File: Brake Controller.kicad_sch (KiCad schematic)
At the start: 21 parts, among them M1 12V, SW1 ENABLE, SW2 HSS, SW3 HSS, U1 IFX007T, U2 IFX007T

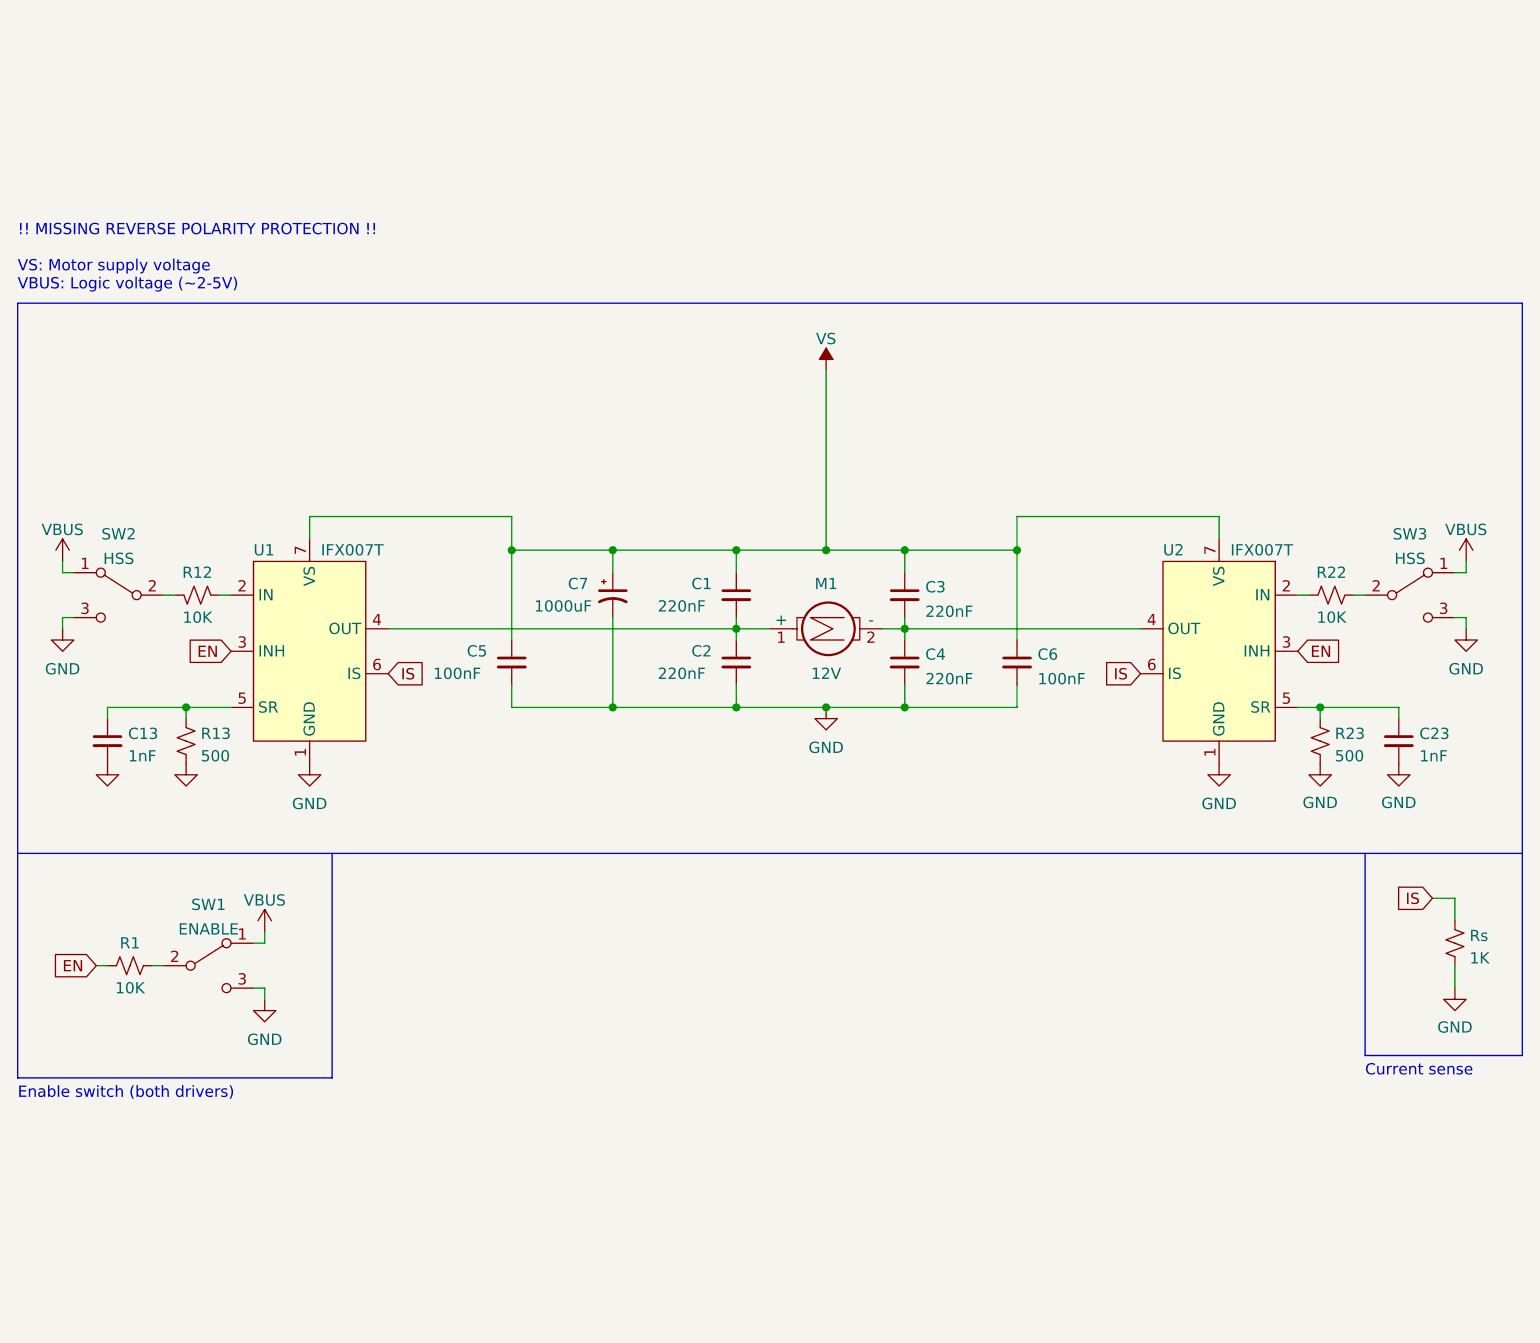
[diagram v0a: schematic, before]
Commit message: Add pin headers, prepare for PCB layout
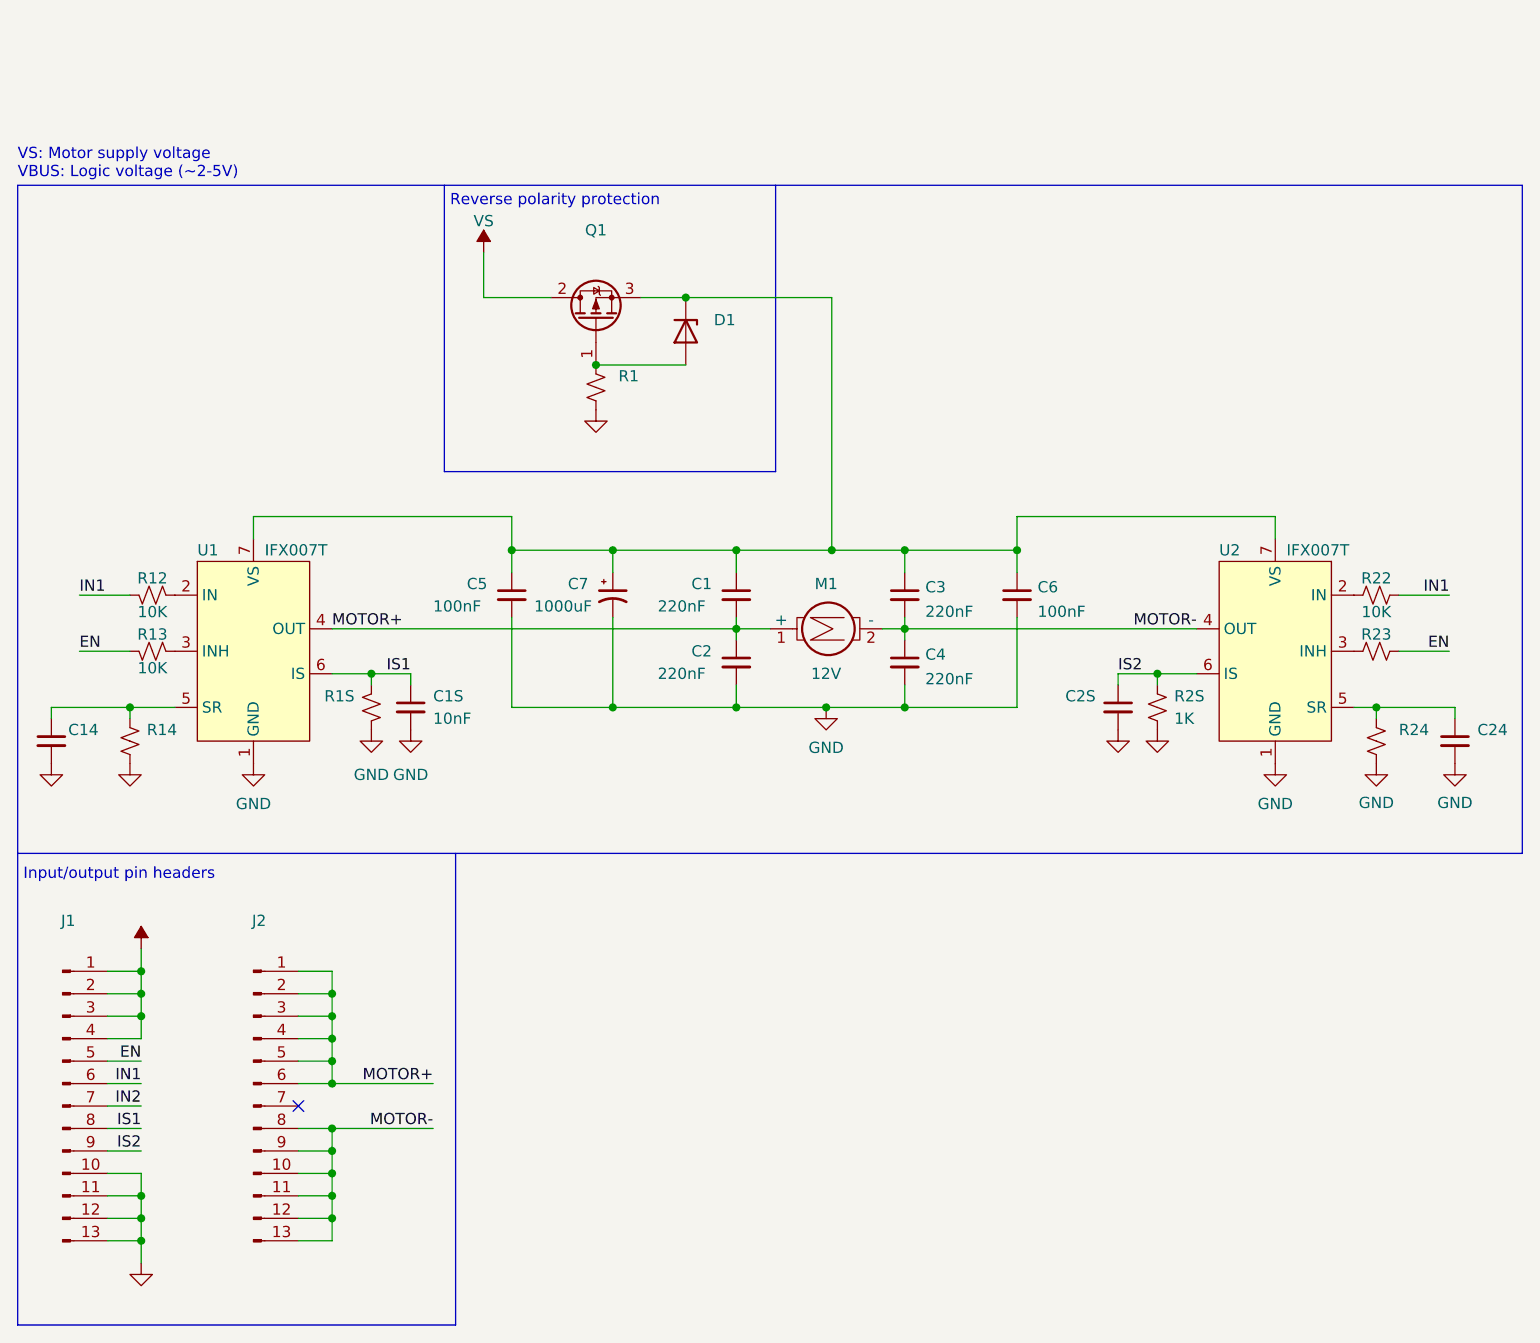
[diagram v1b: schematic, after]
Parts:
- removed C13, C23: 1nF, symbol Device:C_Small
- removed SW1: ENABLE, symbol Switch:SW_SPDT
- removed SW2, SW3: HSS, symbol Switch:SW_SPDT
- added C14, C24, C2S: (no value), symbol Device:C_Small
- added C1S: 10nF, symbol Device:C_Small
- added D1: (no value), symbol Device:D_Zener
- added J1, J2: (no value), symbol Connector:Conn_01x13_Male
- added Q1: (no value), symbol Device:Q_PMOS_GDS
- added R14, R1S, R24: (no value), symbol Device:R_Small_US
- R1: value 10K -> (none)
- R13: value 500 -> 10K
- R23: value 500 -> (none)
- renumbered Rs to R2S
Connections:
- net EN: now also R13.2, R23.2, J1.5 (Pin_5); no longer R1.1, U1.3 (INH), U2.3 (INH)
- net GND: now also R1.2, C14.2, C1S.2, C24.2, C2S.2, J1.10 (Pin_10), J1.11 (Pin_11), J1.12 (Pin_12), J1.13 (Pin_13), R14.2, R1S.2, R24.2; no longer R13.2, R23.2
- net VS: now also J1.1 (Pin_1), J1.2 (Pin_2), J1.3 (Pin_3), J1.4 (Pin_4), Q1.2 (D); no longer C1.1, C3.1, C5.1, C6.1, C7.1, U1.7 (VS), U2.7 (VS)
- net IN1: now reaches R12.2
- net IN1: now also R22.2, J1.6 (Pin_6)
- net at U2.5 (SR): now also C24.1, R24.1; no longer R23.1
- net MOTOR+: now reaches C1.2, C2.1, M1.1 (+), U1.4 (OUT)
- net MOTOR+: now also J2.1 (Pin_1), J2.2 (Pin_2), J2.3 (Pin_3), J2.4 (Pin_4), J2.5 (Pin_5), J2.6 (Pin_6)
- net MOTOR-: now reaches C3.2, C4.1, M1.2 (-), U2.4 (OUT)
- net MOTOR-: now also J2.10 (Pin_10), J2.11 (Pin_11), J2.12 (Pin_12), J2.13 (Pin_13), J2.8 (Pin_8), J2.9 (Pin_9)
- net at U1.5 (SR): now also C14.1, R14.1; no longer R13.1
- net IS renamed IS2
- net IS2: now also C2S.1, J1.9 (Pin_9); no longer U1.6 (IS)
- new net: D1.2 (A), Q1.1 (G), R1.1
- new net: C1.1, C3.1, C5.1, C6.1, C7.1, D1.1 (K), Q1.3 (S), U1.7 (VS), U2.7 (VS)
- new net: R13.1, U1.3 (INH)
- new net: R23.1, U2.3 (INH)
- new net IN2: J1.7 (Pin_7)
- new net IS1: C1S.1, J1.8 (Pin_8), R1S.1, U1.6 (IS)
- no-connect marks 0 -> 1
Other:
- note added: "Input/output pin headers"
- note added: "Reverse polarity protection"
- note added: "VS: Motor supply voltage VBUS: Logic voltage (~2-5V)"
- note removed: "!! MISSING REVERSE POLARITY PROTECTION !! VS: Motor supply voltage VBUS: Logic voltage (~2-5V)"
- note removed: "Current sense"
- note removed: "Enable switch (both drivers)"
- moved on the sheet: C5, C6, R12, R22, R2S, U1, U2

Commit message: Edit author/schematic title
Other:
- company: Ben Owen -> AMP Purdue
- title: IFX007T Motor Driver Testing -> Brake Controller Breakout
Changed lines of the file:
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@@
   (paper "USLetter")
   (title_block
-    (title "IFX007T Motor Driver Testing")
-    (date "2022-01-06")
+    (title "Brake Controller Breakout")
+    (date "2022-04-04")
     (rev "A")
-    (company "Ben Owen")
+    (company "AMP Purdue")
   )
   (junction (at 207.01 104.14) (diameter 0) (color 0 0 0 0)

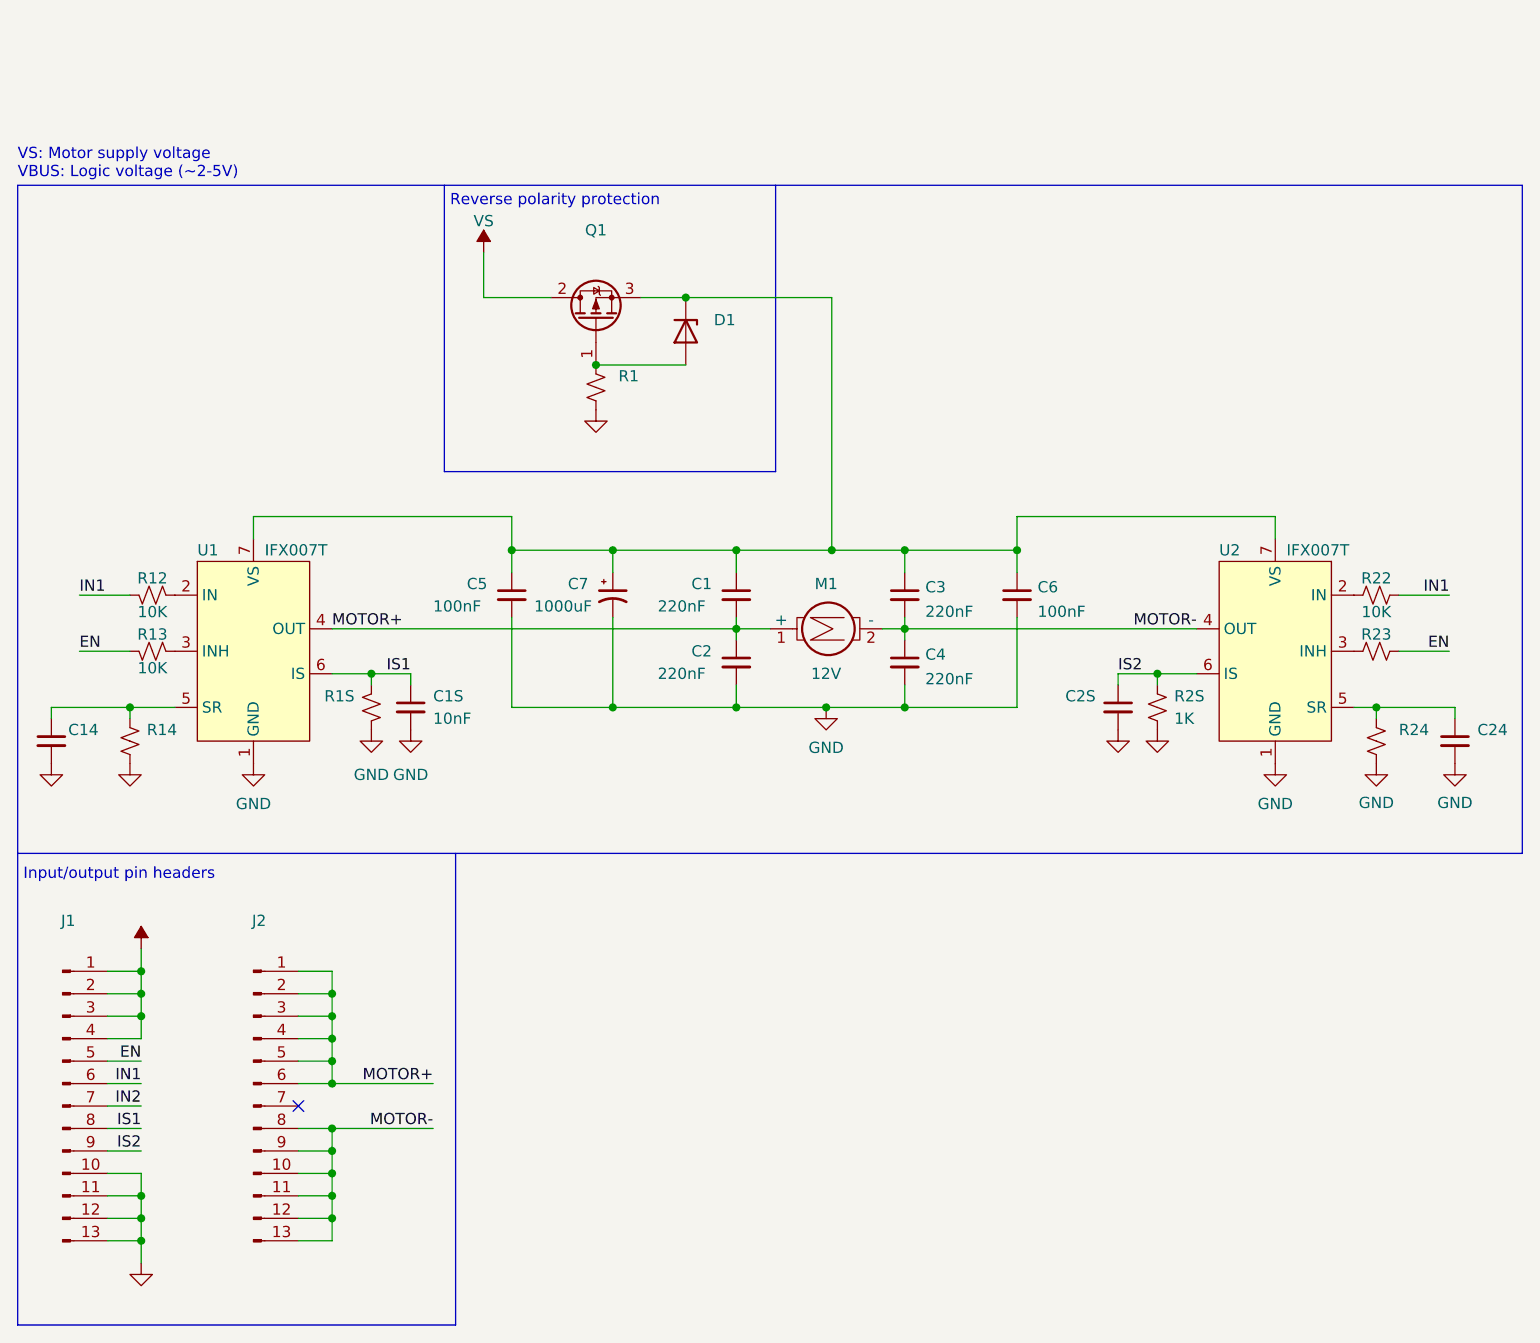
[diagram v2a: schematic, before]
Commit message: Fix missing GND labels
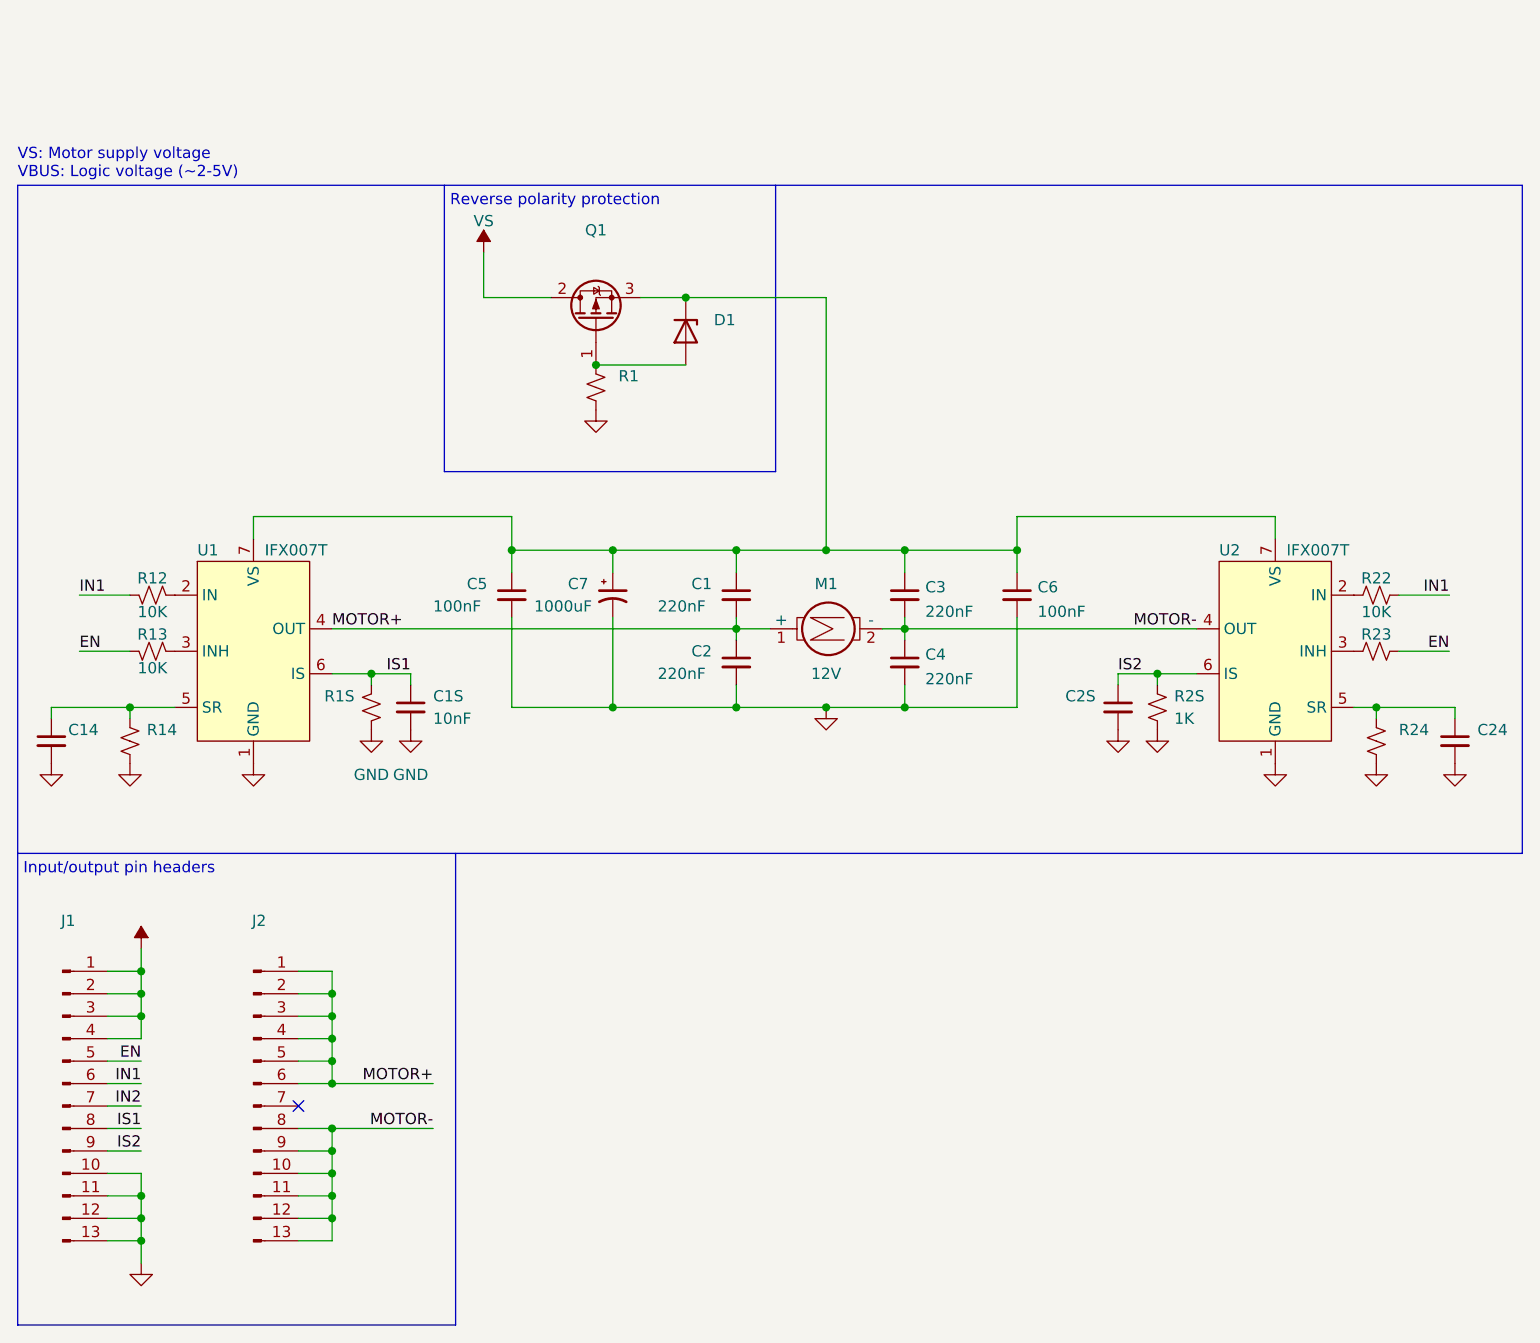
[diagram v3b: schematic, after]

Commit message: Add reverse polarity bypass
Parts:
- removed D1: (no value), symbol Device:D_Zener
- added D1: (no value), symbol Diode:BZX84Cxx
- added JP1: (no value), symbol Jumper:Jumper_2_Open
- C14, C24: value (none) -> 1nF
- C25: renamed from C2S; value (none) -> 10nF
- J1: value (none) -> INPUT
- J2: value (none) -> OUTPUT
- Q1: value (none) -> Q_PMOS_GDS
- R1, R23: value (none) -> 10K
- R14, R24: value (none) -> 500
- R15: renamed from R1S; value (none) -> 1K
- U1, U2: value IFX007T -> (none); footprint (none) -> Package_TO_SOT_SMD:TO-263-7_TabPin4
- renumbered C1S to C15, R2S to R25
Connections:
- net GND: no longer U1.8 (GND), U2.8 (GND)
- net IN1: no longer R22.2
- net IN2: now also R22.2
- net MOTOR+: now also U1.8 (OUT)
- net MOTOR-: now also U2.8 (OUT)
- net VS: now also JP1.1 (A)
- net at Q1.1 (G), R1.1: now also D1.1 (A)
- net at C1.1, C3.1, C5.1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: now also D1.3 (K), JP1.2 (B)
